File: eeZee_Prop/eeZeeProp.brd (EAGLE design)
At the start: 47.2 x 24.4 mm, 28 parts, among them Q1 5MHz, SW1 RESET, U1 P8X32A-Q44, U2 24LC256-I/ST, U3 NCP1117 3V3

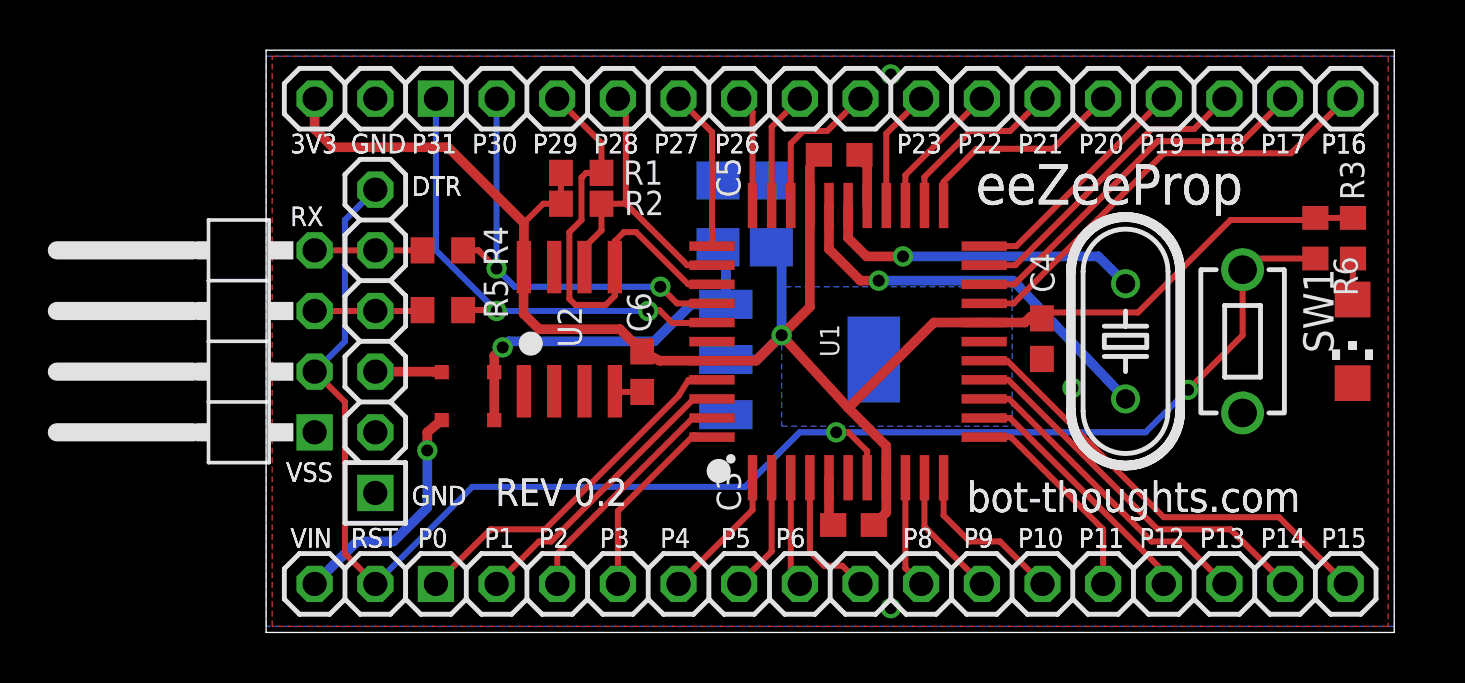
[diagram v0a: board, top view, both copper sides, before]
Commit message: Revised reset circuit, added bypass for VIN diode, added BOE solder jumper
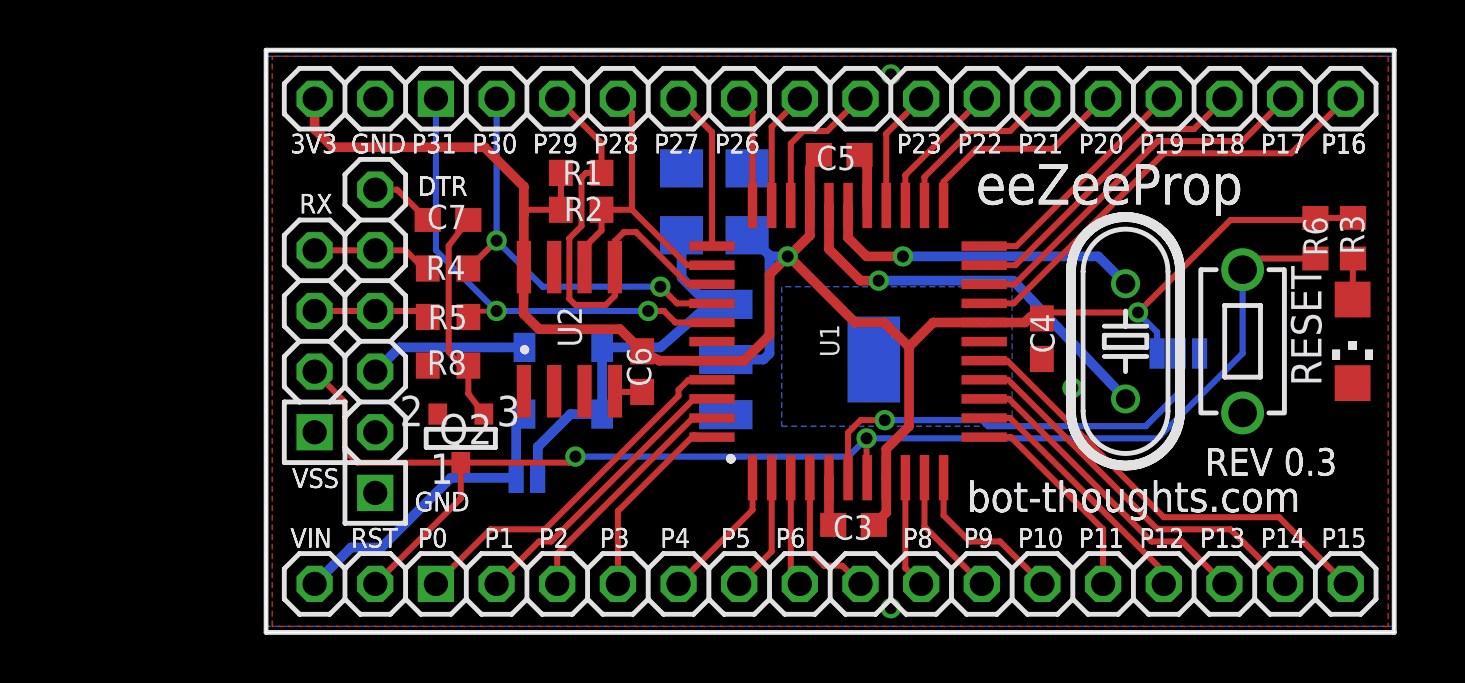
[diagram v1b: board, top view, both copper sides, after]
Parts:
- added C7: 0.1uF, rcl:C0603
- added Q2: 2N3904SMD, mes_transistors:SOT-23
- added R8: 10k, rcl:R0603
- added SJ1: BYPASS, SparkFun:SJ_2S-NO
- added SJ2: !BOE, SparkFun:SJ_3
- D1, D2: value 800mA 10V -> MBR130LSFT1; device diode:SOD323-R -> mes_diode:SOD123FL
- JP3: device pinhead-2:1X04/90-S -> pinhead-2:1X04-S
- JP7: value !RESET -> !RES
- moved D1 5.02 mm to (12.4, 11.9), flipped to the bottom, turned to 0 degrees
- moved D2 4.36 mm to (12.4, 9.14), flipped to the bottom, turned to 0 degrees
- moved JP3 3.81 mm to (2.03, 12.2)
- moved C1 1.61 mm to (17.4, 18.0)
- moved C2 1.14 mm to (20.1, 18.0)
- moved R4 0.79 mm to (7.62, 15.2)
- moved R5 0.37 mm to (7.62, 13.2)
- moved R2 0.25 mm to (13.2, 17.7)
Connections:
- new net !BOE: SJ2.2, U1.6
- new net DTR: C7.2, JP4.6
- new net N$31: C7.1, Q2.3, R8.2
- net !RES: now also Q2.1; no longer JP4.6
- net GND: now also Q2.2, R8.1, SJ2.1; no longer U1.6
- net V+: now also SJ1.2
- net VDD: now also SJ2.3
- net VIN: now also D2.A, SJ1.1; no longer D1.A
- net VUSB: now also D1.A; no longer D2.A
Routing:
- net !BOE: track 0.00 -> 18.3 mm, vias 0 -> 1
- net N$31: track 0.00 -> 9.80 mm
- net !RES: track 68.0 -> 58.5 mm
- net VDD: track 80.1 -> 85.3 mm, vias 1 -> 2
- net VUSB: track 2.78 -> 6.67 mm
- net VIN: track 9.99 -> 13.1 mm, vias 1 -> 0
- net DTR: track 0.00 -> 2.72 mm
- net P30: track 18.5 -> 17.7 mm
- net N$34: track 4.52 -> 5.02 mm
- net V+: vias 1 -> 0
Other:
- board text added: "!BOE"
- board text added: "BYPASS"
- board text added: "RESET"
- board text added: "REV 0.3"
- board text added: "VDD"
- board text removed: "REV 0.2"
